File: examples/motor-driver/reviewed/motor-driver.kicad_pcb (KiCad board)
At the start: 2 copper layers, 88 x 50 mm, 19 parts, among them J1 VM 2.7-10.8V, J2 MOTOR A, J3 MOTOR B, J4 LOGIC, U1 DRV8833PW

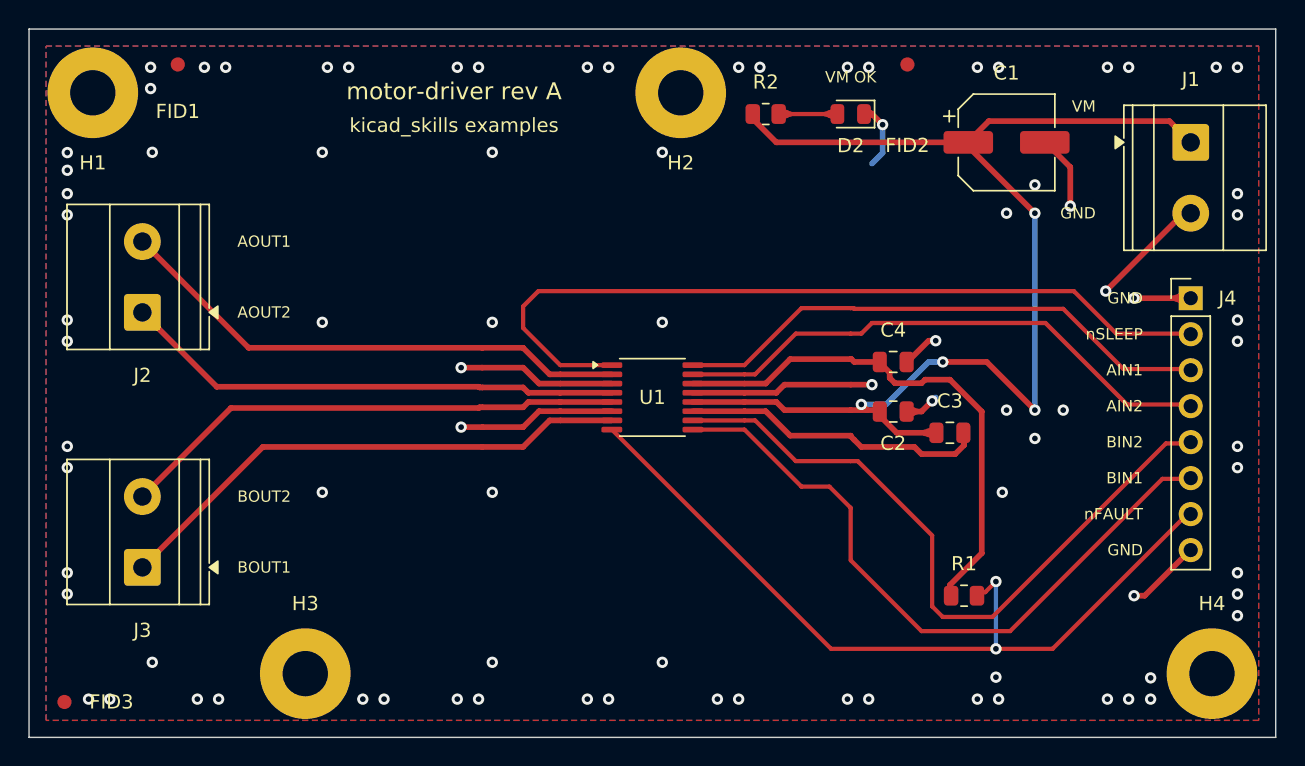
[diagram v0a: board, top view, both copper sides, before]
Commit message: Rebuild golden layouts and gate floorplan quality
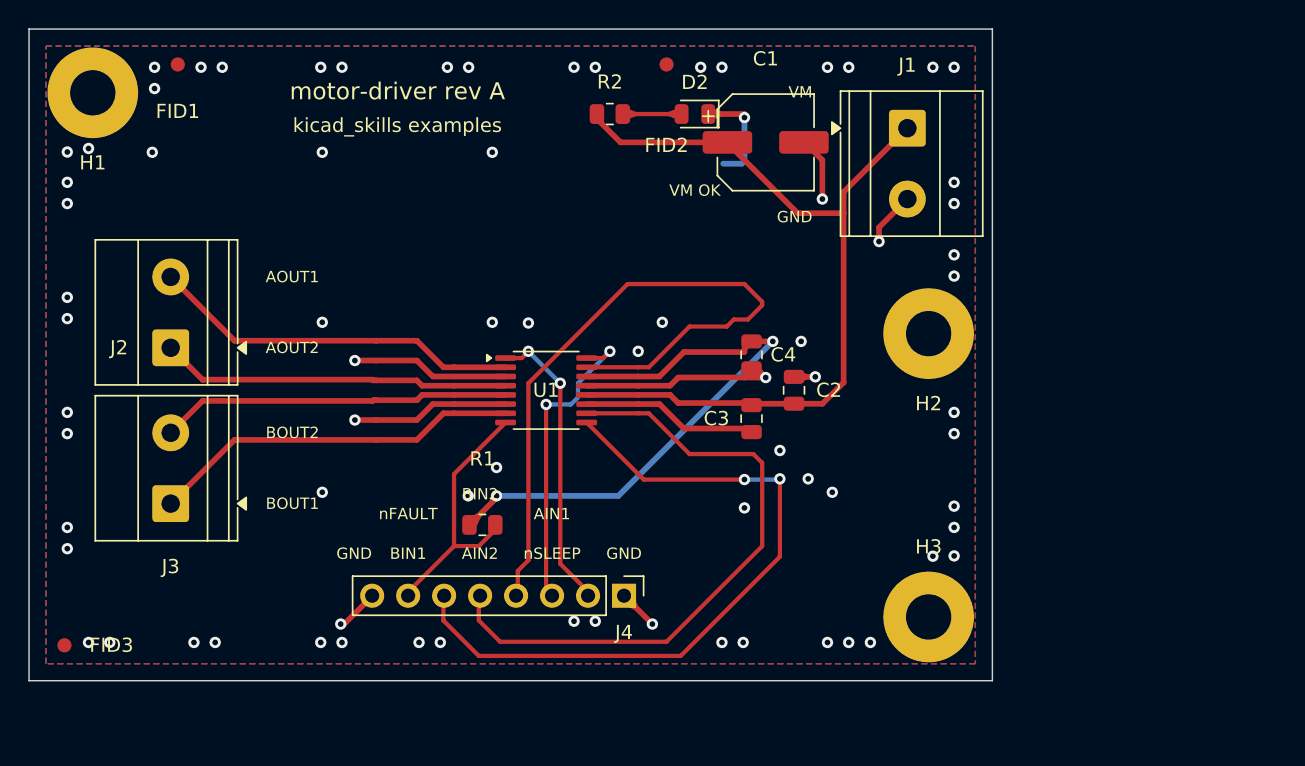
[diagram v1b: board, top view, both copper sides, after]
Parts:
- removed H4: M3, MountingHole:MountingHole_3.2mm_M3_Pad
- moved J4 45.2 mm to (142.0, 100.0), turned to 270 degrees
- moved H3 44.2 mm to (163.5, 101.5)
- moved R1 34.4 mm to (132.0, 95.0)
- moved H2 24.4 mm to (163.5, 81.5)
- moved J1 20.0 mm to (162.0, 67.0)
- moved C1 17.0 mm to (152.0, 68.0)
- moved FID2 17.0 mm to (145.0, 62.5)
- moved C3 14.0 mm to (151.0, 87.5), turned to 270 degrees
- moved D2 11.0 mm to (147.0, 66.0)
- moved R2 11.0 mm to (141.0, 66.0)
- moved C4 10.0 mm to (151.0, 83.0), turned to 270 degrees
- moved U1 7.52 mm to (136.5, 85.5)
- moved C2 7.16 mm to (154.0, 85.5), turned to 90 degrees
- moved J3 4.92 mm to (110.0, 93.5)
- moved FID3 4.00 mm to (102.5, 103.5)
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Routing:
- net /nFAULT: track 57.7 -> 18.9 mm, vias 2 -> 0
- net /nSLEEP: track 57.7 -> 20.8 mm, vias 0 -> 2
- net /VM: track 87.9 -> 59.5 mm, vias 4 -> 0
- net /AIN1: track 38.6 -> 22.9 mm, vias 0 -> 2
- net /BOUT1: track 37.4 -> 26.3 mm
- net /BOUT2: track 35.9 -> 24.7 mm
- net /AOUT2: track 35.5 -> 24.7 mm
- net /AOUT1: track 37.0 -> 26.3 mm
- net /AIN2: track 39.1 -> 49.7 mm
- net /VCP: track 21.6 -> 12.5 mm
- net GND: track 67.8 -> 59.1 mm, vias 88 -> 76
- net /VINT: track 37.1 -> 41.2 mm, vias 0 -> 2
- net /BIN2: track 48.9 -> 44.9 mm
- net /BIN1: track 47.7 -> 50.3 mm, vias 0 -> 2
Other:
- board size 88 x 50 mm -> 68 x 46 mm

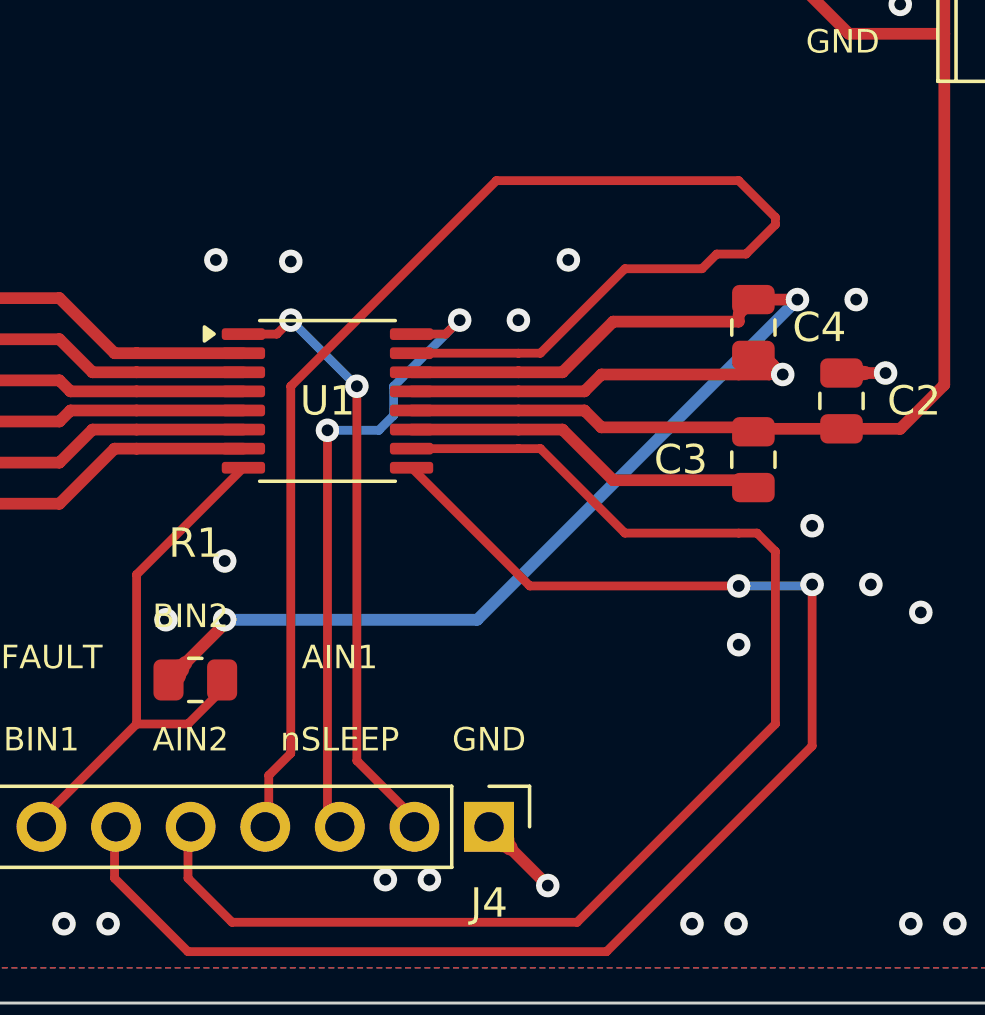
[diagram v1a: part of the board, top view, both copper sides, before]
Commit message: Use canonical fills and close motor return path
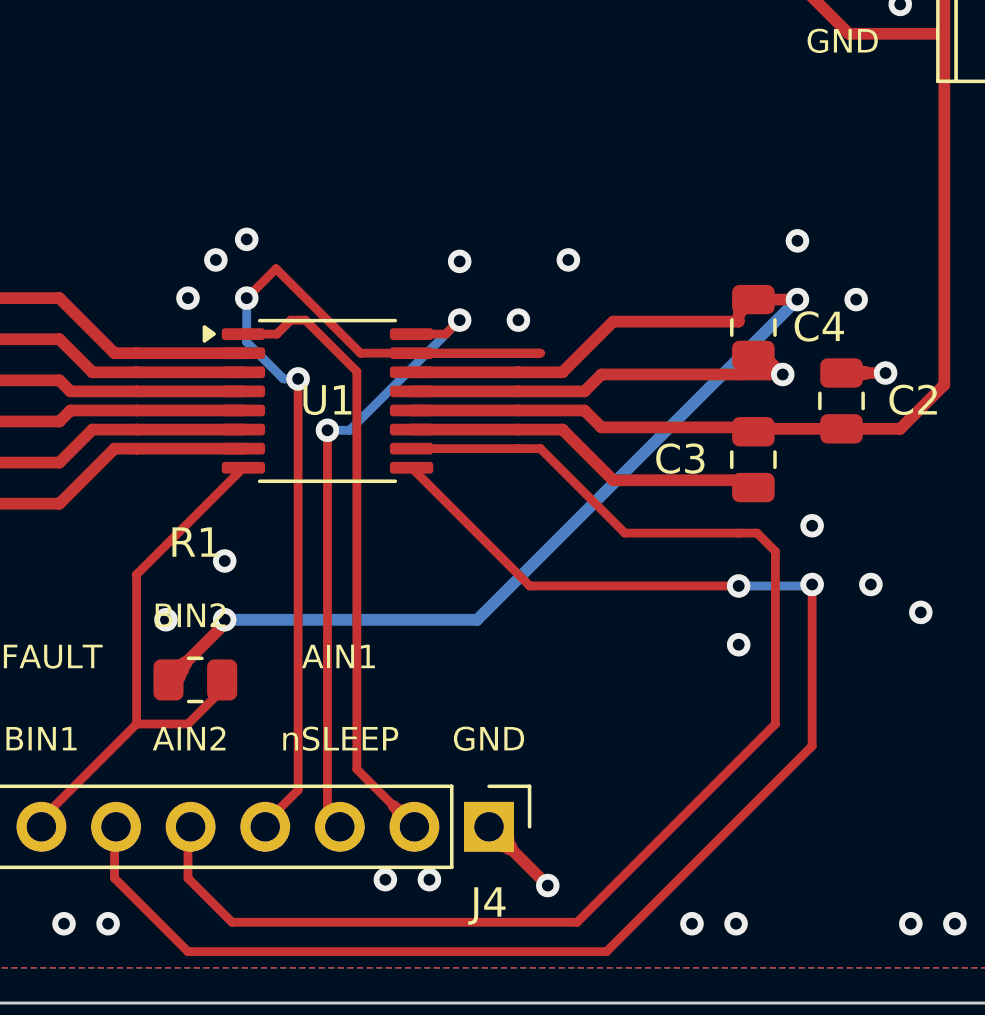
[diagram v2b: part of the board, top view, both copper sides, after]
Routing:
- net /AIN2: track 49.7 -> 35.5 mm, vias 0 -> 2
- net /AIN1: track 22.9 -> 21.6 mm
- net /nSLEEP: track 20.8 -> 21.1 mm, vias 2 -> 0
- net GND: vias 76 -> 79

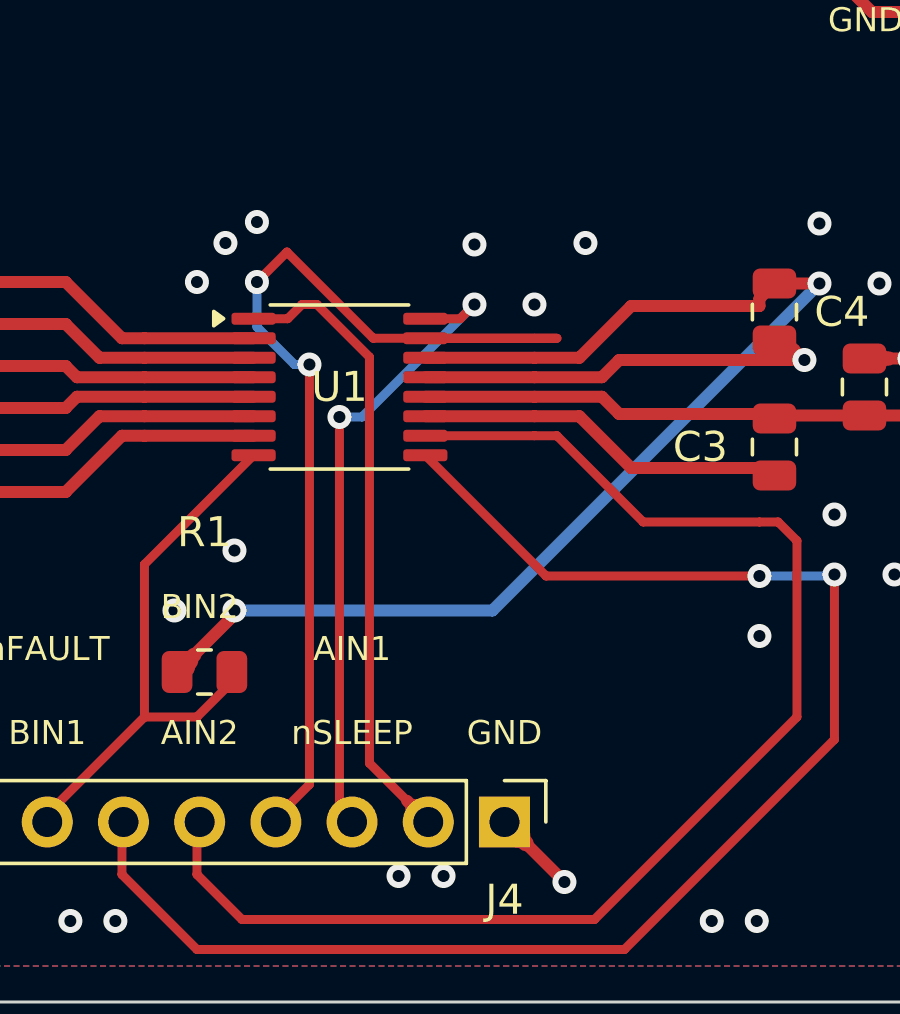
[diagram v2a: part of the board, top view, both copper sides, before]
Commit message: Finalize deterministic golden regeneration
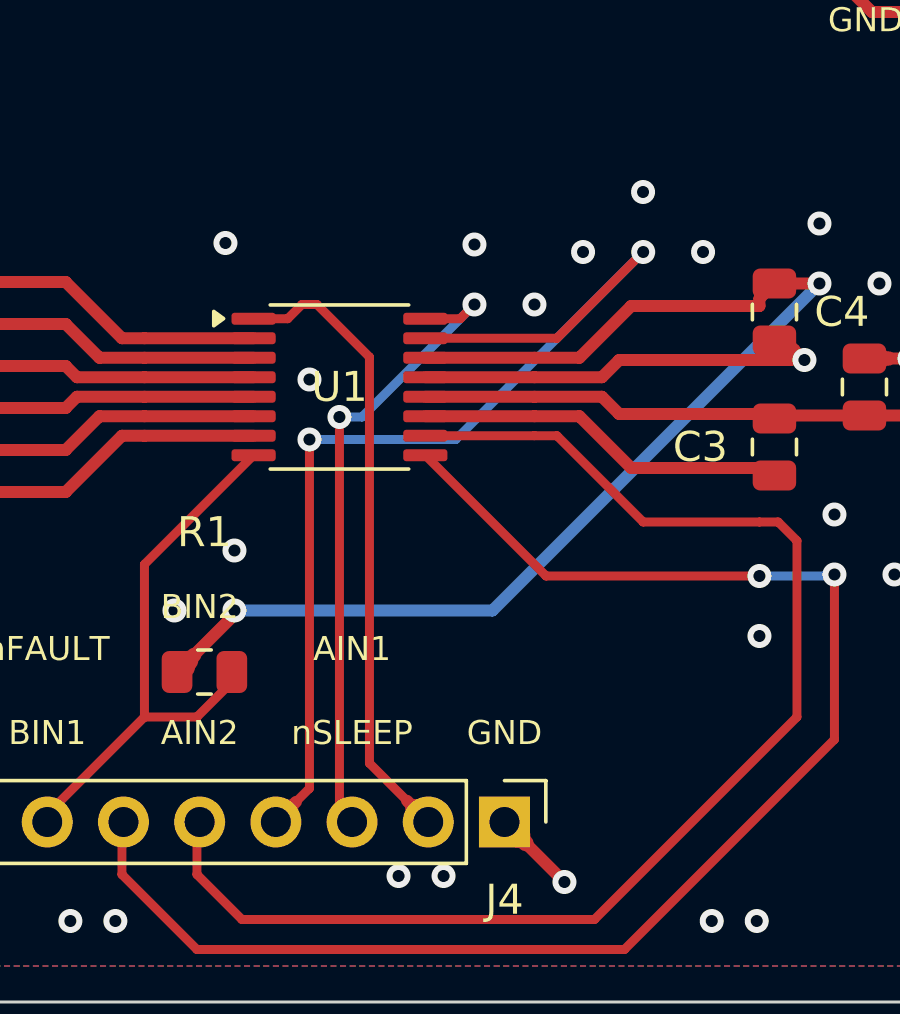
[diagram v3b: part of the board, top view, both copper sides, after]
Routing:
- net GND: vias 79 -> 80
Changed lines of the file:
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@@
 	(segment (start 133.6375 87.775) (end 130.0 91.4125) (width 0.3) (layer "F.Cu") (net 14))
 	(segment (start 130.0 91.4125) (end 130.0 96.5) (width 0.3) (layer "F.Cu") (net 14))
-	(segment (start 139.3625 83.875) (end 143.0 83.875) (width 0.3) (layer "F.Cu") (net 3))
-	(segment (start 143.0 83.875) (end 143.75 83.875) (width 0.3) (layer "F.Cu") (net 3))
-	(segment (start 143.75 83.875) (end 137.625 83.875) (width 0.3) (layer "F.Cu") (net 3))
-	(segment (start 137.625 83.875) (end 134.75 81.0) (width 0.3) (layer "F.Cu") (net 3))
-	(segment (start 134.75 81.0) (end 133.75 82.0) (width 0.3) (layer "F.Cu") (net 3))
 	(segment (start 139.3625 84.525) (end 143.0 84.525) (width 0.4) (layer "F.Cu") (net 12))
 	(segment (start 143.0 84.525) (end 144.5 84.525) (width 0.4) (layer "F.Cu") (net 12))
@@
 	(segment (start 139.3625 83.225) (end 140.525 83.225) (width 0.3) (layer "F.Cu") (net 2))
 	(segment (start 140.525 83.225) (end 141.0 82.75) (width 0.3) (layer "F.Cu") (net 2))
+	(segment (start 139.3625 83.875) (end 143.75 83.875) (width 0.3) (layer "F.Cu") (net 3))
+	(segment (start 143.75 83.875) (end 146.625 81.0) (width 0.3) (layer "F.Cu") (net 3))
 	(segment (start 161.2929 67.7071) (end 157.5 71.5) (width 0.4) (layer "F.Cu") (net 13))
 	(segment (start 157.5 71.5) (end 157.5 73.0) (width 0.4) (layer "F.Cu") (net 13))
@@
 	(segment (start 136.5 86.5) (end 136.5 99.58) (width 0.3) (layer "F.Cu") (net 2))
 	(segment (start 136.5 99.58) (end 136.668 99.748) (width 0.3) (layer "F.Cu") (net 2))
-	(segment (start 133.75 82.0) (end 133.75 83.5) (width 0.3) (layer "B.Cu") (net 3))
-	(segment (start 133.75 83.5) (end 135.0 84.75) (width 0.3) (layer "B.Cu") (net 3))
-	(segment (start 135.0 84.75) (end 135.5 84.75) (width 0.3) (layer "B.Cu") (net 3))
-	(segment (start 135.5 84.75) (end 135.5 98.75) (width 0.3) (layer "F.Cu") (net 3))
-	(segment (start 135.5 98.75) (end 134.5 99.75) (width 0.3) (layer "F.Cu") (net 3))
-	(segment (start 134.5 99.75) (end 134.5 99.88) (width 0.3) (layer "F.Cu") (net 3))
-	(segment (start 134.5 99.88) (end 134.38 100.0) (width 0.3) (layer "F.Cu") (net 3))
+	(segment (start 146.625 81.0) (end 140.375 87.25) (width 0.3) (layer "B.Cu") (net 3))
+	(segment (start 140.375 87.25) (end 135.5 87.25) (width 0.3) (layer "B.Cu") (net 3))
+	(segment (start 135.5 87.25) (end 135.5 98.88) (width 0.3) (layer "F.Cu") (net 3))
+	(segment (start 135.5 98.88) (end 135.052 99.328) (width 0.3) (layer "F.Cu") (net 3))
 	(segment (start 150.5 91.8) (end 152.95 91.8) (width 0.3) (layer "B.Cu") (net 6))
 	(segment (start 152.95 91.8) (end 153.0 91.75) (width 0.3) (layer "B.Cu") (net 6))
@@
 	(segment (start 136.836 99.916) (end 136.752 99.832) (width 0.6) (layer "F.Cu") (net 2))
 	(segment (start 136.752 99.832) (end 136.668 99.748) (width 0.4) (layer "F.Cu") (net 2))
+	(segment (start 134.38 100.0) (end 134.604 99.776) (width 0.8) (layer "F.Cu") (net 3))
+	(segment (start 134.604 99.776) (end 134.828 99.552) (width 0.6) (layer "F.Cu") (net 3))
+	(segment (start 134.828 99.552) (end 135.052 99.328) (width 0.4) (layer "F.Cu") (net 3))
 	(segment (start 139.46 100.0) (end 139.2243 99.7643) (width 0.8) (layer "F.Cu") (net 15))
 	(segment (start 139.2243 99.7643) (end 138.9886 99.5286) (width 0.6) (layer "F.Cu") (net 15))
@@
 	(via (at 141.0 82.75) (size 0.8) (drill 0.4) (layers "F.Cu" "B.Cu") (net 2))
 	(via (at 136.5 86.5) (size 0.8) (drill 0.4) (layers "F.Cu" "B.Cu") (net 2))
+	(via (at 146.625 81.0) (size 0.8) (drill 0.4) (layers "F.Cu" "B.Cu") (net 3))
+	(via (at 135.5 87.25) (size 0.8) (drill 0.4) (layers "F.Cu" "B.Cu") (net 3))
 	(via (at 150.5 91.8) (size 0.8) (drill 0.4) (layers "F.Cu" "B.Cu") (net 6))
 	(via (at 144.0 102.0) (size 0.8) (drill 0.4) (layers "F.Cu" "B.Cu") (net 1))
@@
 	(via (at 156.0 72.0) (size 0.8) (drill 0.4) (layers "F.Cu" "B.Cu") (net 1))
 	(via (at 153.0 91.75) (size 0.8) (drill 0.4) (layers "F.Cu" "B.Cu") (net 6))
-	(via (at 133.75 82.0) (size 0.8) (drill 0.4) (layers "F.Cu" "B.Cu") (net 3))
-	(via (at 135.5 84.75) (size 0.8) (drill 0.4) (layers "F.Cu" "B.Cu") (net 3))
 	(via (at 104.2 103.3) (size 0.8) (drill 0.4) (layers "F.Cu" "B.Cu") (net 1))
 	(via (at 112.14 62.7) (size 0.8) (drill 0.4) (layers "F.Cu" "B.Cu") (net 1))
@@
 	(via (at 133.0 90.95) (size 0.8) (drill 0.4) (layers "F.Cu" "B.Cu") (net 1))
 	(via (at 143.0 82.75) (size 0.8) (drill 0.4) (layers "F.Cu" "B.Cu") (net 1))
-	(via (at 131.75 82.0) (size 0.8) (drill 0.4) (layers "F.Cu" "B.Cu") (net 1))
-	(via (at 133.75 80.0) (size 0.8) (drill 0.4) (layers "F.Cu" "B.Cu") (net 1))
+	(via (at 141.0 80.75) (size 0.8) (drill 0.4) (layers "F.Cu" "B.Cu") (net 1))
+	(via (at 148.62 81.0) (size 0.8) (drill 0.4) (layers "F.Cu" "B.Cu") (net 1))
+	(via (at 144.62 81.0) (size 0.8) (drill 0.4) (layers "F.Cu" "B.Cu") (net 1))
+	(via (at 146.62 79.0) (size 0.8) (drill 0.4) (layers "F.Cu" "B.Cu") (net 1))
+	(via (at 135.5 85.25) (size 0.8) (drill 0.4) (layers "F.Cu" "B.Cu") (net 1))
 	(via (at 150.5 93.8) (size 0.8) (drill 0.4) (layers "F.Cu" "B.Cu") (net 1))
 	(via (at 155.0 91.75) (size 0.8) (drill 0.4) (layers "F.Cu" "B.Cu") (net 1))
@@
 	(via (at 108.86 64.2) (size 0.8) (drill 0.4) (layers "F.Cu" "B.Cu") (net 1))
 	(via (at 104.2 68.43) (size 0.8) (drill 0.4) (layers "F.Cu" "B.Cu") (net 1))
-	(via (at 141.0 80.75) (size 0.8) (drill 0.4) (layers "F.Cu" "B.Cu") (net 1))
-	(via (at 144.7 80.7) (size 0.8) (drill 0.4) (layers "F.Cu" "B.Cu") (net 1))
 	(zone
 		(net 1)

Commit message: Clear final motor layout blockers
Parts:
- moved D2 2.00 mm to (145.0, 66.0)
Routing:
- net /AIN2: track 35.4 -> 39.2 mm, vias 2 -> 1
- net GND: track 59.1 -> 56.7 mm
- net /LED_A: track 4.15 -> 2.15 mm
- net /VM: track 59.5 -> 60.4 mm
